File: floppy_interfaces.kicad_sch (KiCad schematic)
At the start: 24 parts, among them J13 Conn_01x04_Male, J14 Conn_02x17_Odd_Even, J16 Conn_01x04_Male, J6 SDF-60J for IEC 1541 serial p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, U1 74LS373, U2 74LVC374, U22 74LS06N, U3 74LVC374, U4 74LS373

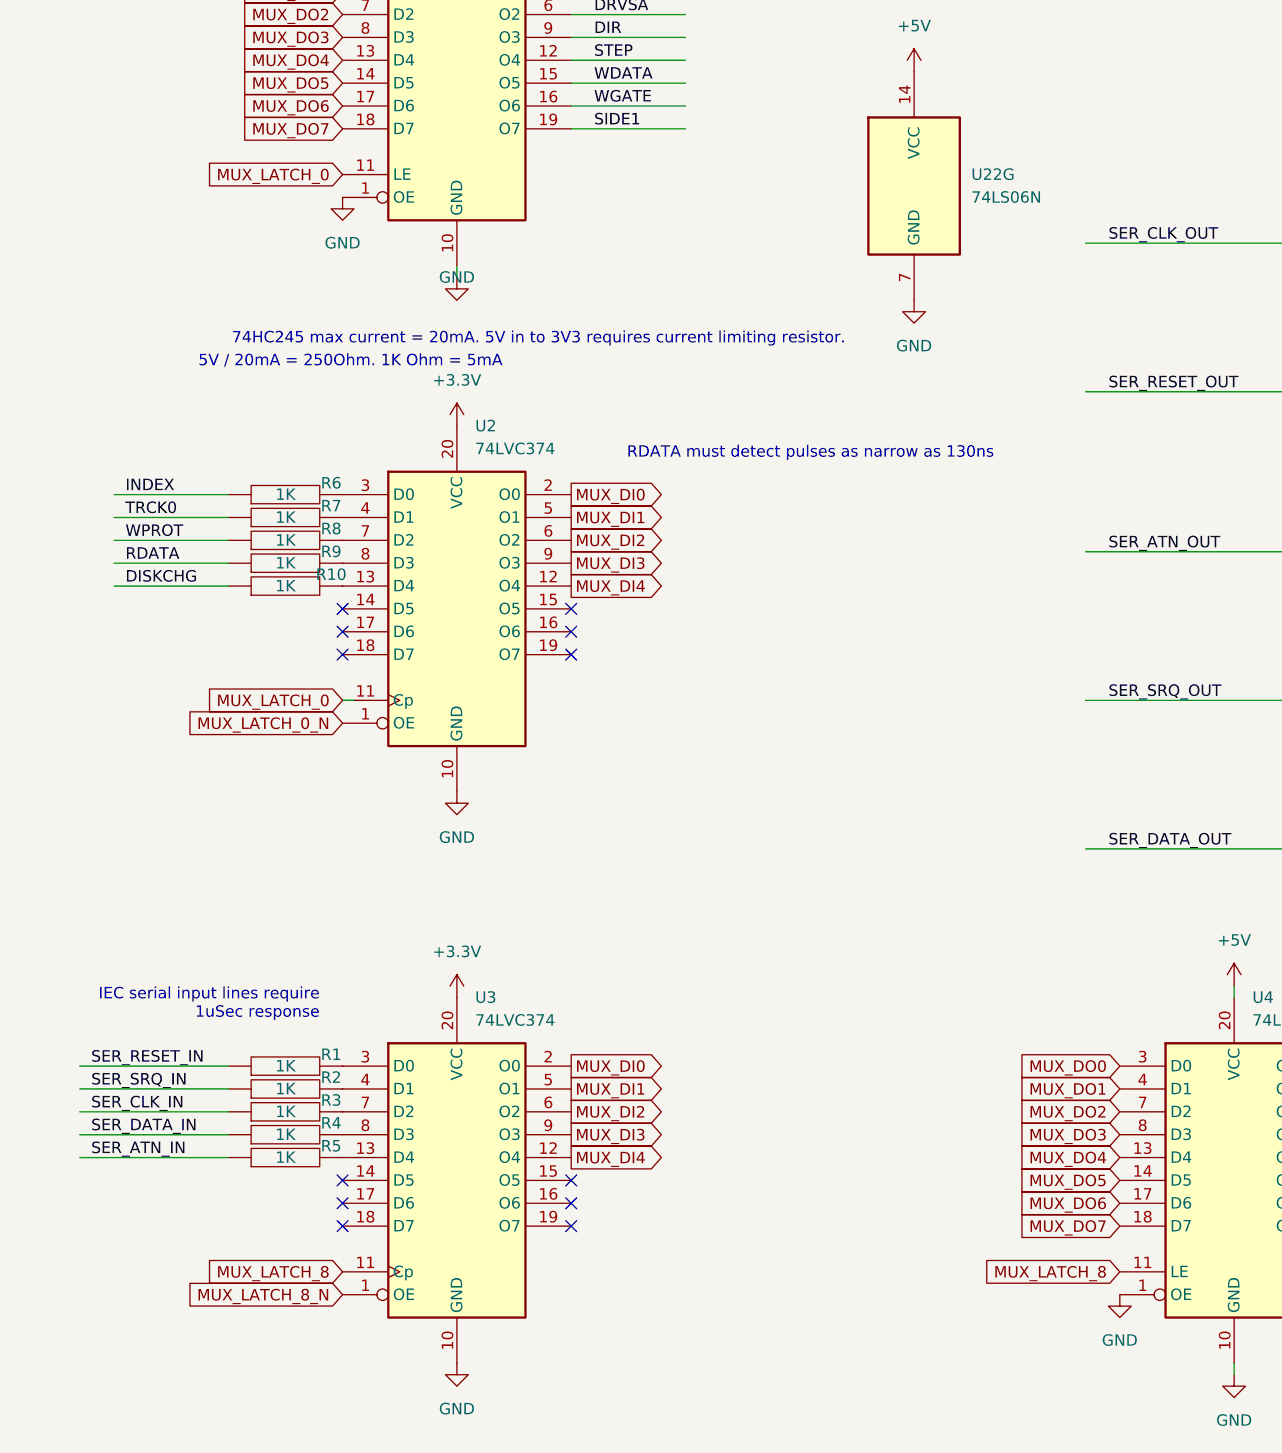
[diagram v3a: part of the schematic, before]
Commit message: route hi MUX address lines
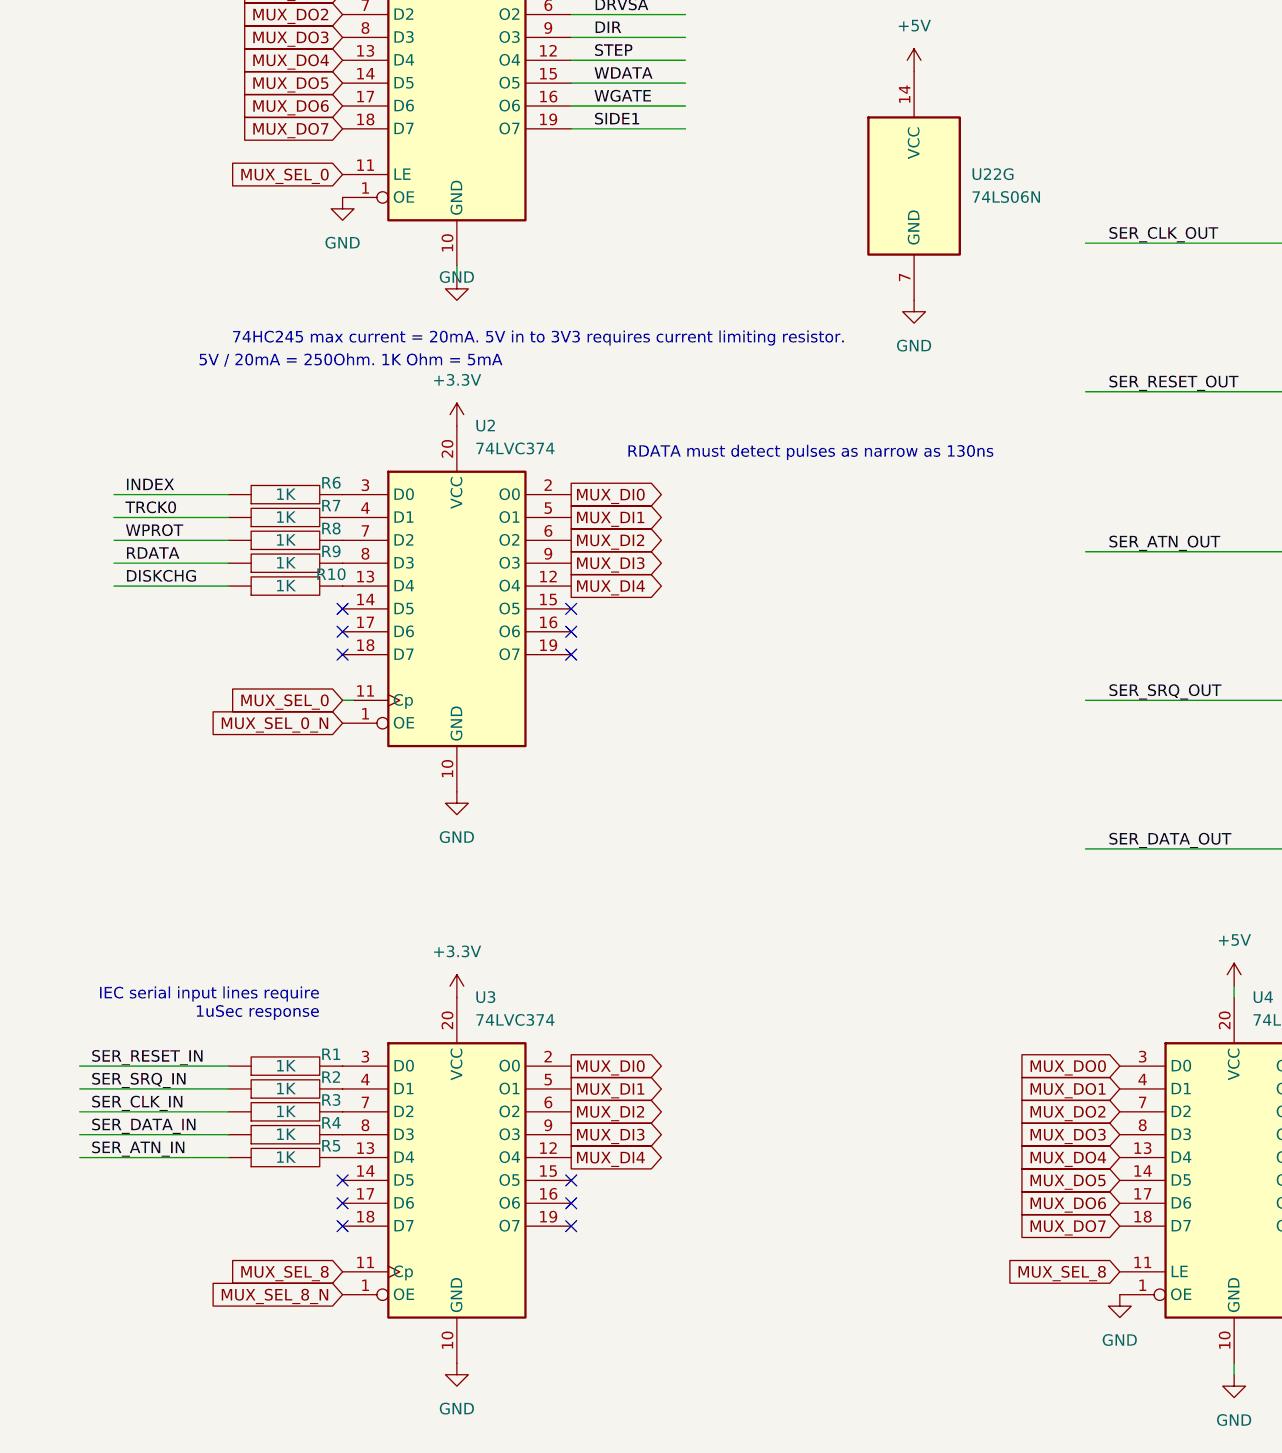
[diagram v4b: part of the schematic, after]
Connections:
- net MUX_LATCH_0 renamed MUX_SEL_0
- net MUX_LATCH_0_N renamed MUX_SEL_0_N
- net MUX_LATCH_8 renamed MUX_SEL_8
- net MUX_LATCH_8_N renamed MUX_SEL_8_N
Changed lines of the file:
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@@
     )
   )
-  (global_label "MUX_LATCH_8" (shape input) (at 130.81 176.53 180) (fields_autoplaced)
+  (global_label "MUX_SEL_8" (shape input) (at 130.81 176.53 180) (fields_autoplaced)
     (effects (font (size 1.27 1.27)) (justify right))
-    (property "Intersheet References" "${INTERSHEET_REFS}" (id 0) (at 115.5759 176.4506 0)
+    (property "Intersheet References" "${INTERSHEET_REFS}" (id 0) (at 117.874 176.4506 0)
       (effects (font (size 1.27 1.27)) (justify right) hide)
     )
@@
     )
   )
-  (global_label "MUX_LATCH_0" (shape input) (at 44.45 54.61 180) (fields_autoplaced)
+  (global_label "MUX_SEL_0" (shape input) (at 44.45 54.61 180) (fields_autoplaced)
     (effects (font (size 1.27 1.27)) (justify right))
-    (property "Intersheet References" "${INTERSHEET_REFS}" (id 0) (at 29.2159 54.5306 0)
+    (property "Intersheet References" "${INTERSHEET_REFS}" (id 0) (at 31.514 54.5306 0)
       (effects (font (size 1.27 1.27)) (justify right) hide)
     )
@@
     )
   )
-  (global_label "MUX_LATCH_0" (shape input) (at 44.45 113.03 180) (fields_autoplaced)
+  (global_label "MUX_SEL_0" (shape input) (at 44.45 113.03 180) (fields_autoplaced)
     (effects (font (size 1.27 1.27)) (justify right))
-    (property "Intersheet References" "${INTERSHEET_REFS}" (id 0) (at 29.2159 112.9506 0)
+    (property "Intersheet References" "${INTERSHEET_REFS}" (id 0) (at 31.514 112.9506 0)
       (effects (font (size 1.27 1.27)) (justify right) hide)
     )
   )
-  (global_label "MUX_LATCH_8" (shape input) (at 44.45 176.53 180) (fields_autoplaced)
+  (global_label "MUX_SEL_8" (shape input) (at 44.45 176.53 180) (fields_autoplaced)
     (effects (font (size 1.27 1.27)) (justify right))
-    (property "Intersheet References" "${INTERSHEET_REFS}" (id 0) (at 29.2159 176.4506 0)
+    (property "Intersheet References" "${INTERSHEET_REFS}" (id 0) (at 31.514 176.4506 0)
       (effects (font (size 1.27 1.27)) (justify right) hide)
     )
@@
     )
   )
-  (global_label "MUX_LATCH_0_N" (shape input) (at 44.45 115.57 180) (fields_autoplaced)
+  (global_label "MUX_SEL_0_N" (shape input) (at 44.45 115.57 180) (fields_autoplaced)
     (effects (font (size 1.27 1.27)) (justify right))
-    (property "Intersheet References" "${INTERSHEET_REFS}" (id 0) (at 26.9179 115.4906 0)
+    (property "Intersheet References" "${INTERSHEET_REFS}" (id 0) (at 29.2159 115.4906 0)
       (effects (font (size 1.27 1.27)) (justify right) hide)
     )
@@
     )
   )
-  (global_label "MUX_LATCH_8_N" (shape input) (at 44.45 179.07 180) (fields_autoplaced)
+  (global_label "MUX_SEL_8_N" (shape input) (at 44.45 179.07 180) (fields_autoplaced)
     (effects (font (size 1.27 1.27)) (justify right))
-    (property "Intersheet References" "${INTERSHEET_REFS}" (id 0) (at 26.9179 178.9906 0)
+    (property "Intersheet References" "${INTERSHEET_REFS}" (id 0) (at 29.2159 178.9906 0)
       (effects (font (size 1.27 1.27)) (justify right) hide)
     )
